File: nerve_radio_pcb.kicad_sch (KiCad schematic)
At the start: 25 parts, among them J1 BF030-20A-B1-0360-0277-0600-LB, J2 5V GPIO Breakout, J3 3V SPI Breakout, J4 Battery, U1 TXB0104QPWRQ1, U2 TPSM82903, U3 XBP9B-DMWT-002

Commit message: Fix previous bad commit 14902c5
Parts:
- J1: footprint connectors:bf030-20a-b1-0600-0277-0600-lb -> connectors:bf030-20a-b1-0360-0277-0600-lb
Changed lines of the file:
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@@
 		(dnp no)
 		(fields_autoplaced yes)
-		(property "Reference" "#PWR015"
+		(property "Reference" "#PWR014"
 			(at 63.5 54.61 0)
 			(effects
@@
 			(project "nerve_radio_pcb"
 				(path "/c0277862-b3f2-4e0e-986f-34702f0543f0"
-					(reference "#PWR015")
+					(reference "#PWR014")
 					(unit 1)
 				)
@@
 		(dnp no)
 		(fields_autoplaced yes)
-		(property "Reference" "#FLG02"
+		(property "Reference" "#FLG01"
 			(at 28.575 29.21 0)
 			(effects
@@
 			(project "nerve_radio_pcb"
 				(path "/c0277862-b3f2-4e0e-986f-34702f0543f0"
-					(reference "#FLG02")
+					(reference "#FLG01")
 					(unit 1)
 				)
@@
 		(on_board yes)
 		(dnp no)
-		(property "Reference" "#FLG01"
+		(property "Reference" "#FLG02"
 			(at 108.585 31.75 0)
 			(effects
@@
 			(project "nerve_radio_pcb"
 				(path "/c0277862-b3f2-4e0e-986f-34702f0543f0"
-					(reference "#FLG01")
+					(reference "#FLG02")
 					(unit 1)
 				)
@@
 		(dnp no)
 		(fields_autoplaced yes)
-		(property "Reference" "#PWR027"
+		(property "Reference" "#PWR026"
 			(at 234.95 153.67 0)
 			(effects
@@
 			(project "nerve_radio_pcb"
 				(path "/c0277862-b3f2-4e0e-986f-34702f0543f0"
-					(reference "#PWR027")
+					(reference "#PWR026")
 					(unit 1)
 				)
@@
 	)
 	(symbol
-		(lib_id "connectors:bf030-20a-b1-0360-0277-0600-lb")
-		(at 44.45 38.1 0)
-		(mirror y)
-		(unit 1)
-		(exclude_from_sim no)
-		(in_bom yes)
-		(on_board yes)
-		(dnp no)
-		(property "Reference" "J1"
-			(at 44.45 24.13 0)
-			(effects
-				(font
-					(size 1.27 1.27)
-				)
-			)
-		)
-		(property "Value" "BF030-20A-B1-0360-0277-0600-LB"
-			(at 44.45 24.13 0)
-			(effects
-				(font
-					(size 1.27 1.27)
-				)
-				(hide yes)
-			)
-		)
-		(property "Footprint" "connectors:bf030-20a-b1-0600-0277-0600-lb"
-			(at 44.45 38.1 0)
-			(effects
-				(font
-					(size 1.27 1.27)
-				)
-				(hide yes)
-			)
-		)
-		(property "Datasheet" "https://gct.co/files/drawings/bf030.pdf"
-			(at 44.45 38.1 0)
-			(effects
-				(font
-					(size 1.27 1.27)
-				)
-				(hide yes)
-			)
-		)
-		(property "Description" "Connector Header Surface Mount 20 position 0.079\" (2.00mm)"
-			(at 80.01 36.83 0)
-			(effects
-				(font
-					(size 1.27 1.27)
-				)
-				(hide yes)
-			)
-		)
-		(property "Manufacturer" "GCT"
-			(at 44.45 38.1 0)
-			(effects
-				(font
-					(size 1.27 1.27)
-				)
-				(hide yes)
-			)
-		)
-		(property "Manufacturer Part Number" "BF030-20A-B1-0360-0277-0600-LB"
-			(at 44.45 38.1 0)
-			(effects
-				(font
-					(size 1.27 1.27)
-				)
-				(hide yes)
-			)
-		)
-		(property "Distributor" "DigiKey"
-			(at 44.45 38.1 0)
-			(effects
-				(font
-					(size 1.27 1.27)
-				)
-				(hide yes)
-			)
-		)
-		(property "Distributor Part Number" "2073-BF030-20A-B1-0360-0277-0600-LBCT-ND"
-			(at 44.45 38.1 0)
-			(effects
-				(font
-					(size 1.27 1.27)
-				)
-				(hide yes)
-			)
-		)
-		(property "Distributor Link" "https://www.digikey.ca/en/products/detail/gct/BF030-20A-B1-0360-0277-0600-LB/16396935"
-			(at 44.45 38.1 0)
-			(effects
-				(font
-					(size 1.27 1.27)
-				)
-				(hide yes)
-			)
-		)
-		(pin "5"
-		)
-		(pin "20"
-		)
-		(pin "9"
-		)
-		(pin "14"
-		)
-		(pin "3"
-		)
-		(pin "17"
-		)
-		(pin "8"
-		)
-		(pin "13"
-		)
-		(pin "12"
-		)
-		(pin "15"
-		)
-		(pin "6"
-		)
-		(pin "19"
-		)
-		(pin "4"
-		)
-		(pin "1"
-		)
-		(pin "18"
-		)
-		(pin "7"
-		)
-		(pin "2"
-		)
-		(pin "11"
-		)
-		(pin "10"
-		)
-		(pin "16"
-		)
-		(instances
-			(project "nerve_radio_pcb"
-				(path "/c0277862-b3f2-4e0e-986f-34702f0543f0"
-					(reference "J1")
-					(unit 1)
-				)
-			)
-		)
-	)
-	(symbol
 		(lib_id "power:+3V3")
 		(at 57.15 27.94 0)
@@
 		(on_board yes)
 		(dnp no)
-		(property "Reference" "#PWR08"
+		(property "Reference" "#PWR06"
 			(at 57.15 31.75 0)
 			(effects
@@
 			(project "nerve_radio_pcb"
 				(path "/c0277862-b3f2-4e0e-986f-34702f0543f0"
-					(reference "#PWR08")
+					(reference "#PWR06")
 					(unit 1)
 				)
@@
 		(dnp no)
 		(fields_autoplaced yes)
-		(property "Reference" "#PWR014"
+		(property "Reference" "#PWR013"
 			(at 210.82 52.07 0)
 			(effects
@@
 			(project "nerve_radio_pcb"
 				(path "/c0277862-b3f2-4e0e-986f-34702f0543f0"
-					(reference "#PWR014")
+					(reference "#PWR013")
 					(unit 1)
 				)
@@
 		(dnp no)
 		(fields_autoplaced yes)
-		(property "Reference" "#PWR013"
+		(property "Reference" "#PWR015"
 			(at 157.48 54.61 0)
 			(effects
@@
 			(project "nerve_radio_pcb"
 				(path "/c0277862-b3f2-4e0e-986f-34702f0543f0"
-					(reference "#PWR013")
+					(reference "#PWR015")
 					(unit 1)
 				)
@@
 		(on_board yes)
 		(dnp no)
-		(property "Reference" "#PWR05"
+		(property "Reference" "#PWR07"
 			(at 111.76 34.29 0)
 			(effects
@@
 			(project "nerve_radio_pcb"
 				(path "/c0277862-b3f2-4e0e-986f-34702f0543f0"
-					(reference "#PWR05")
+					(reference "#PWR07")
 					(unit 1)
 				)
@@
 	)
 	(symbol
+		(lib_id "connectors:bf030-20a-b1-0360-0277-0600-lb")
+		(at 44.45 38.1 0)
+		(mirror y)
+		(unit 1)
+		(exclude_from_sim no)
+		(in_bom yes)
+		(on_board yes)
+		(dnp no)
+		(property "Reference" "J1"
+			(at 44.45 24.13 0)
+			(effects
+				(font
+					(size 1.27 1.27)
+				)
+			)
+		)
+		(property "Value" "BF030-20A-B1-0360-0277-0600-LB"
+			(at 44.45 22.86 0)
+			(effects
+				(font
+					(size 1.27 1.27)
+				)
+				(hide yes)
+			)
+		)
+		(property "Footprint" "connectors:bf030-20a-b1-0360-0277-0600-lb"
+			(at 44.45 38.1 0)
+			(effects
+				(font
+					(size 1.27 1.27)
+				)
+				(hide yes)
+			)
+		)
+		(property "Datasheet" "https://gct.co/files/drawings/bf030.pdf"
+			(at 44.45 38.1 0)
+			(effects
+				(font
+					(size 1.27 1.27)
+				)
+				(hide yes)
+			)
+		)
+		(property "Description" "Connector Header Surface Mount 20 position 0.079\" (2.00mm)"
+			(at 80.01 36.83 0)
+			(effects
+				(font
+					(size 1.27 1.27)
+				)
+				(hide yes)
+			)
+		)
+		(property "Manufacturer" "GCT"
+			(at 44.45 38.1 0)
+			(effects
+				(font
+					(size 1.27 1.27)
+				)
+				(hide yes)
+			)
+		)
+		(property "Manufacturer Part Number" "BF030-20A-B1-0360-0277-0600-LB"
+			(at 44.45 38.1 0)
+			(effects
+				(font
+					(size 1.27 1.27)
+				)
+				(hide yes)
+			)
+		)
+		(property "Distributor" "DigiKey"
+			(at 44.45 38.1 0)
+			(effects
+				(font
+					(size 1.27 1.27)
+				)
+				(hide yes)
+			)
+		)
+		(property "Distributor Part Number" "2073-BF030-20A-B1-0360-0277-0600-LBCT-ND"
+			(at 44.45 38.1 0)
+			(effects
+				(font
+					(size 1.27 1.27)
+				)
+				(hide yes)
+			)
+		)
+		(property "Distributor Link" "https://www.digikey.ca/en/products/detail/gct/BF030-20A-B1-0360-0277-0600-LB/16396935"
+			(at 44.45 38.1 0)
+			(effects
+				(font
+					(size 1.27 1.27)
+				)
+				(hide yes)
+			)
+		)
+		(pin "2"
+		)
+		(pin "6"
+		)
+		(pin "12"
+		)
+		(pin "18"
+		)
+		(pin "7"
+		)
+		(pin "1"
+		)
+		(pin "20"
+		)
+		(pin "9"
+		)
+		(pin "4"
+		)
+		(pin "13"
+		)
+		(pin "15"
+		)
+		(pin "3"
+		)
+		(pin "5"
+		)
+		(pin "17"
+		)
+		(pin "8"
+		)
+		(pin "14"
+		)
+		(pin "10"
+		)
+		(pin "11"
+		)
+		(pin "19"
+		)
+		(pin "16"
+		)
+		(instances
+			(project ""
+				(path "/c0277862-b3f2-4e0e-986f-34702f0543f0"
+					(reference "J1")
+					(unit 1)
+				)
+			)
+		)
+	)
+	(symbol
 		(lib_id "Device:R")
 		(at 157.48 43.18 0)
@@
 		(on_board yes)
 		(dnp no)
-		(property "Reference" "#PWR06"
+		(property "Reference" "#PWR08"
 			(at 152.4 34.29 0)
 			(effects
@@
 			(project "nerve_radio_pcb"
 				(path "/c0277862-b3f2-4e0e-986f-34702f0543f0"
-					(reference "#PWR06")
+					(reference "#PWR08")
 					(unit 1)
 				)
@@
 		(on_board yes)
 		(dnp no)
-		(property "Reference" "#PWR07"
+		(property "Reference" "#PWR05"
 			(at 31.75 31.75 0)
 			(effects
@@
 			(project "nerve_radio_pcb"
 				(path "/c0277862-b3f2-4e0e-986f-34702f0543f0"
-					(reference "#PWR07")
+					(reference "#PWR05")
 					(unit 1)
 				)
@@
 		(dnp no)
 		(fields_autoplaced yes)
-		(property "Reference" "#PWR026"
+		(property "Reference" "#PWR027"
 			(at 57.15 156.21 0)
 			(effects
@@
 			(project "nerve_radio_pcb"
 				(path "/c0277862-b3f2-4e0e-986f-34702f0543f0"
-					(reference "#PWR026")
+					(reference "#PWR027")
 					(unit 1)
 				)

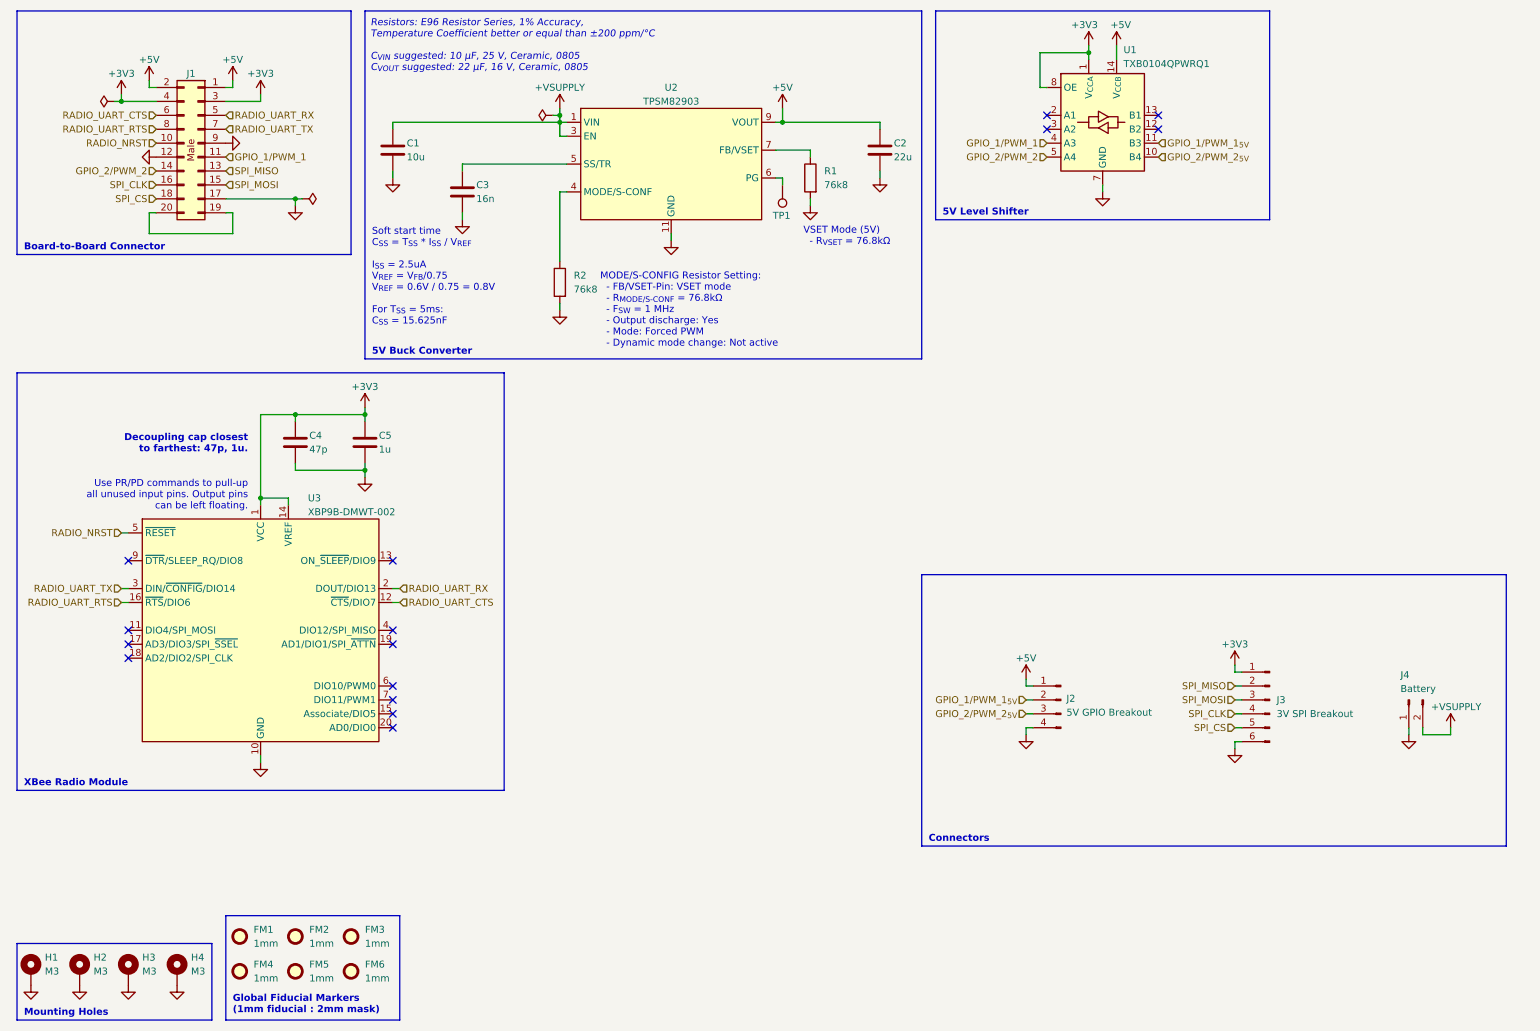
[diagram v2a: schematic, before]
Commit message: Update buck converter for v1.0.0 dev
- Update component library
- Change buck regulator design to LMR51430
- Cleanup PCB
- Update version info
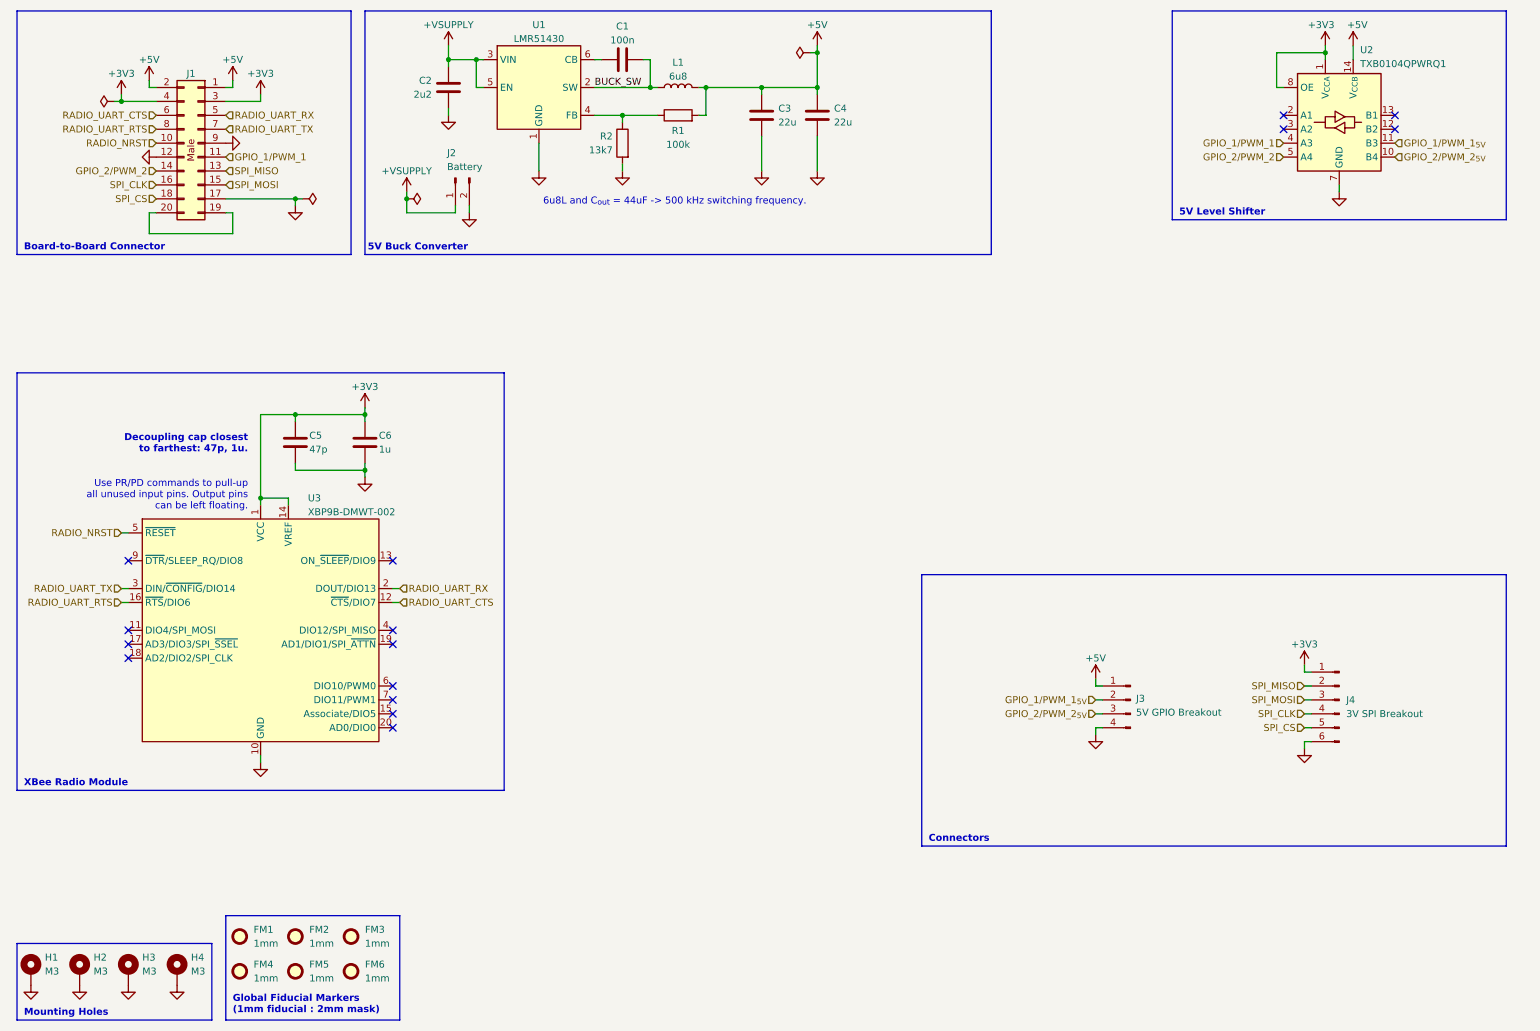
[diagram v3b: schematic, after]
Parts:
- removed J4: Battery, radio_pcb_connectors:battery, symbol Connector:Conn_01x02_Pin
- removed TP1: TestPoint, TestPoint:TestPoint_Pad_D2.0mm, symbol Connector:TestPoint
- removed U2: TPSM82903, ti_buck:tpsm8290x, symbol ti_buck:tpsm82903
- added C4: 22u, Capacitor_SMD:C_1210_3225Metric, symbol Device:C
- added J2: Battery, radio_pcb_connectors:battery, symbol Connector:Conn_01x02_Pin
- added L1: 6u8, radio_pcb_inductors:vishay_ihlp-2525cz, symbol Device:L
- added U1: LMR51430, ti_buck:lmr51430, symbol ti_buck:lmr51430
- C1: value 10u -> 100n
- C2: value 22u -> 2u2
- C3: value 16n -> 22u; footprint Capacitor_SMD:C_0603_1608Metric -> Capacitor_SMD:C_1210_3225Metric
- R1: value 76k8 -> 100k
- R2: value 76k8 -> 13k7
- renumbered C4 to C5, C5 to C6, J2 to J3, J3 to J4, U1 to U2
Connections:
- net +5V: now also C3.2, R1.2, C4.2, L1.2; no longer C2.1
- net +VSUPPLY: now also C2.1, J2.1 (Pin_1), U1.3 (VIN), U1.5 (EN); no longer C1.1
- net GND: now also C3.1, C4.1, J2.2 (Pin_2), U1.1 (GND); no longer C1.2, C3.2, R1.2
- net at R2.1: now also R1.1, U1.4 (FB)
- new net: C1.1, U1.6 (CB)
- new net BUCK_SW: C1.2, L1.1, U1.2 (SW)
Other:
- note added: "6u8L and C_{out} = 44uF -> 500 kHz switching frequency."
- note removed: "MODE/S-CONFIG Resistor Setting: - FB/VSET-Pin: VSET mode - R_{MODE/S-CONF} = 76.8kΩ - F_{SW} = 1 MHz - Output discharge: Yes - Mode: Forced PWM - Dynamic mode change: Not active"
- note removed: "Resistors: E96 Resistor Series, 1% Accuracy, Temperature Coefficient better or equal than ±200 ppm/°C C_{VIN} suggested: 10 μF, 25 V, Ceramic, 0805 C_{VOUT} suggested: 22 μF, 16 V, Ceramic, 0805"
- note removed: "Soft start time C_{SS} = T_{SS} * I_{SS} / V_{REF} I_{SS} = 2.5uA V_{REF} = V_{FB}/0.75 V_{REF} = 0.6V / 0.75 = 0.8V For T_{SS} = 5ms: C_{SS} = 15.625nF"
- note removed: "VSET Mode (5V) - R_{VSET} = 76.8kΩ"
- moved on the sheet: J3, J4, U2

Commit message: Update for KiCad 9.0 and component library
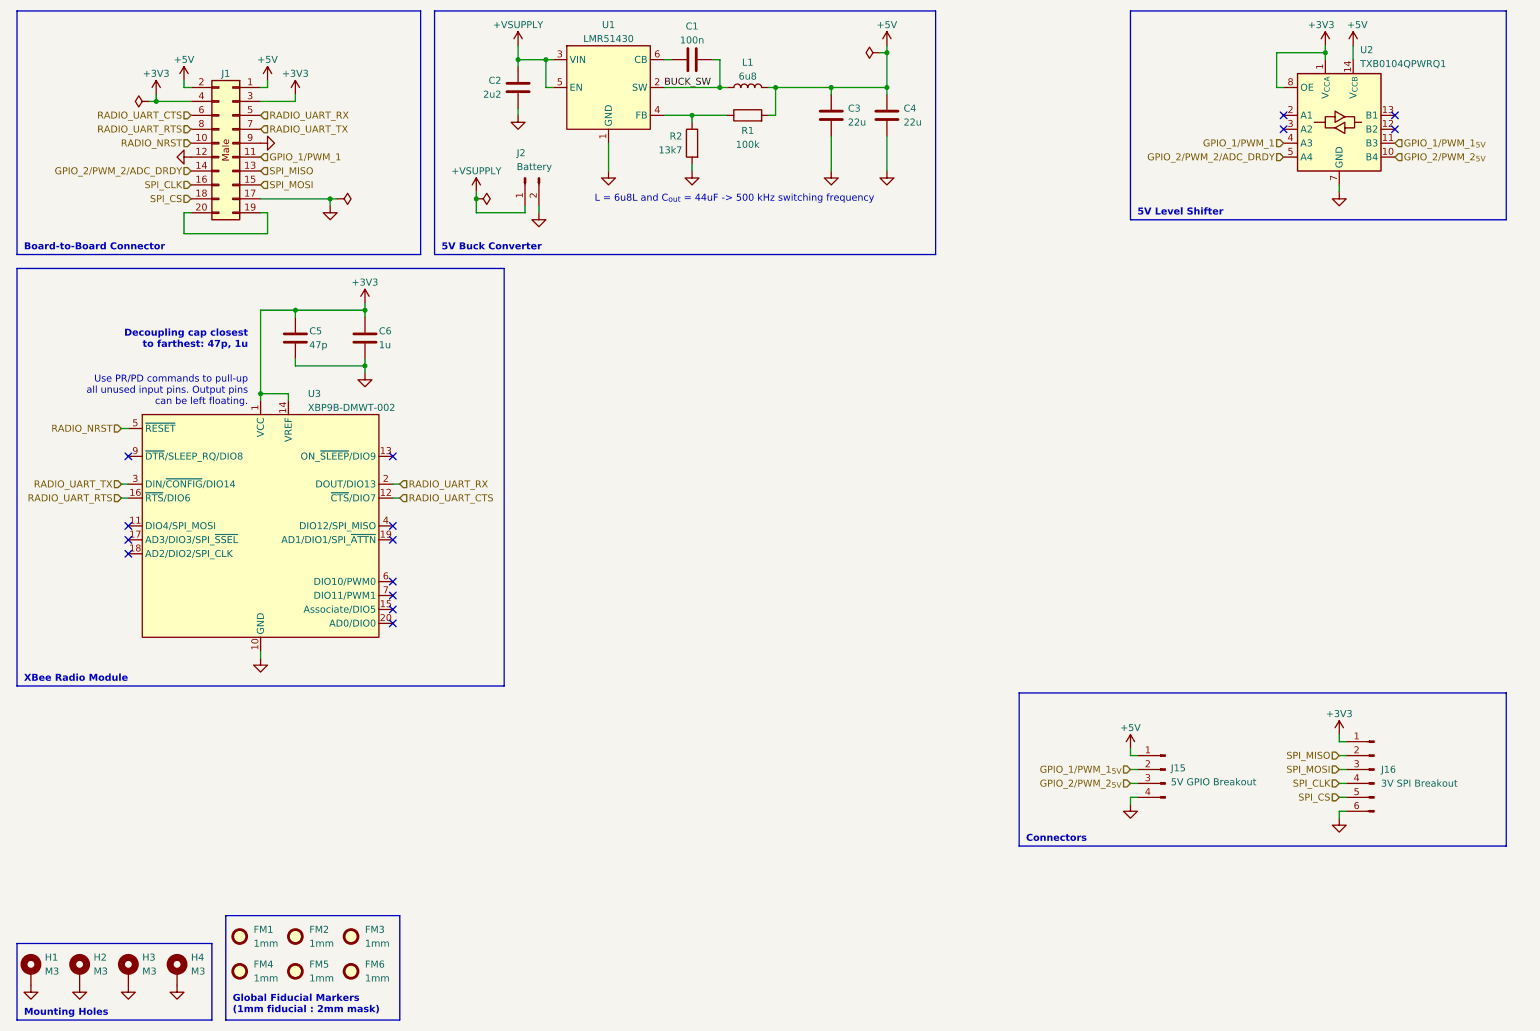
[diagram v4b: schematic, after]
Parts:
- renumbered J3 to J15, J4 to J16
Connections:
- net GPIO_2/PWM_2 renamed GPIO_2/PWM_2/ADC_DRDY
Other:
- note added: "Decoupling cap closest to farthest: 47p, 1u"
- note added: "L = 6u8L and C_{out} = 44uF -> 500 kHz switching frequency"
- note removed: "6u8L and C_{out} = 44uF -> 500 kHz switching frequency."
- note removed: "Decoupling cap closest to farthest: 47p, 1u."
- moved on the sheet: C1, C2, C3, C4, C5, C6, J1, J15, J16, J2, L1, R1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
